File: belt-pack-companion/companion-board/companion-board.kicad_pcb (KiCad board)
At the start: 2 copper layers, 29.4 x 47.2 mm, 64 parts, among them J1 Conn_01x18_Socket, J2 Conn_01x18_Socket, J4 Conn_01x03_Pin, Q1 MMBT3904, Q2 MMBT3904, U1 TLV320AIC3204, X1 YC24.576MUBCE2O

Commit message: PCB Updates
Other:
- board text added: "Heltec WiFi LoRa 32 v3 Companion Board Rev.1"
- board text added: "Heltec v3 Companion Rev.1"
- board text added: "Line Out"

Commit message: Board updates
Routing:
- net GND: vias 156 -> 153
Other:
- board text added: "Supported by"
- board text added: "https://github.com/PKCubed/LibreCom"

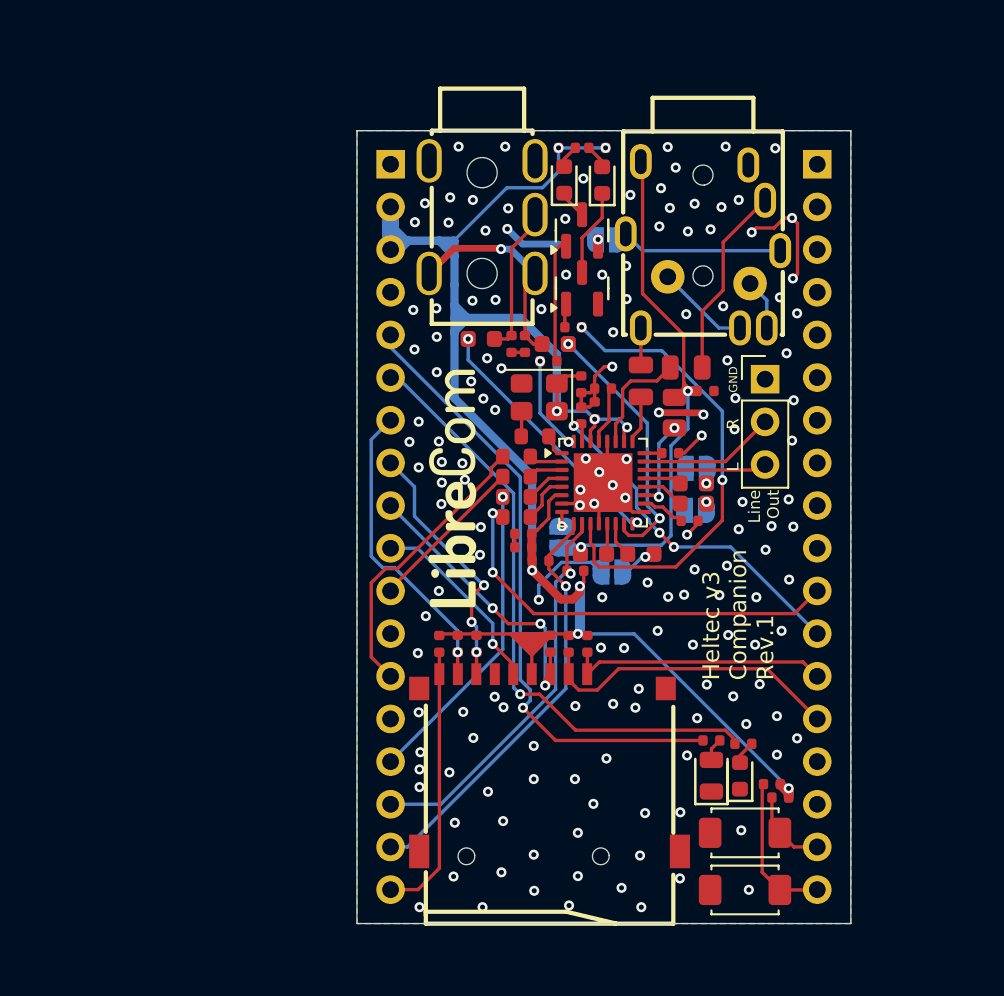
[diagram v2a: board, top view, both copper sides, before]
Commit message: Added more GPIO labels and started to add PTT button
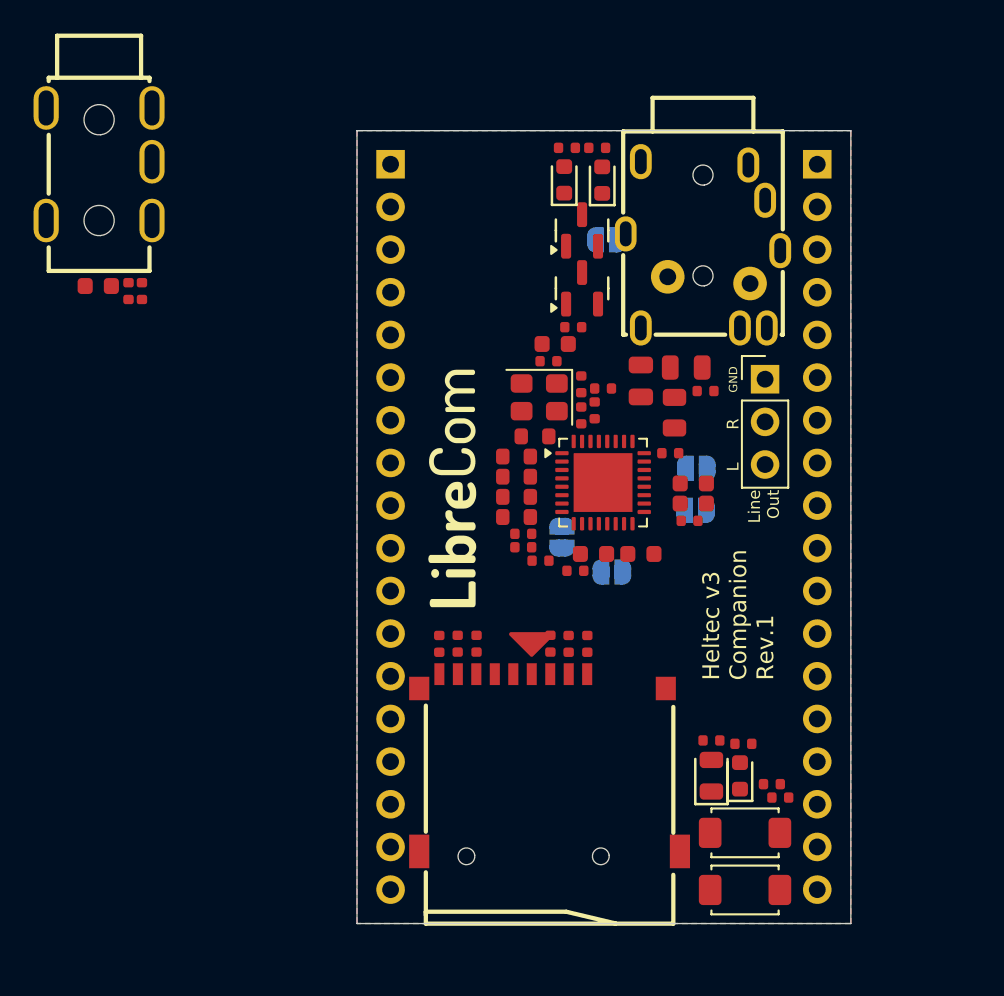
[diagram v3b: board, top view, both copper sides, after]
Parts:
- moved R33 23.0 mm to (95.1, 48.0)
- moved J3 23.0 mm to (93.3, 40.5)
- moved R32 23.0 mm to (95.9, 48.0)
- moved C11 23.0 mm to (93.3, 47.8)
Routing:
- net +3.3V: track 109.6 -> 0.00 mm, vias 9 -> 0
- net GND: track 39.8 -> 0.00 mm, vias 153 -> 0
- net LED_Green: track 37.3 -> 0.00 mm, vias 1 -> 0
- net LED_Red: track 36.4 -> 0.00 mm, vias 1 -> 0
- net MIC: track 34.6 -> 0.00 mm, vias 2 -> 0
- net Net-(U1-MISO/MFP4): track 28.2 -> 0.00 mm, vias 2 -> 0
- net I^{2}C_SCL: track 25.2 -> 0.00 mm, vias 1 -> 0
- net I^{2}S_MIC_DATA: track 25.1 -> 0.00 mm, vias 2 -> 0
- net I^{2}C_SDA: track 23.6 -> 0.00 mm, vias 1 -> 0
- net CODEC_RESET: track 21.9 -> 0.00 mm, vias 3 -> 0
- net I^{2}S_SPK_DATA: track 18.5 -> 0.00 mm, vias 1 -> 0
- net SD_DAT3: track 18.5 -> 0.00 mm
- net SD_DAT1: track 18.2 -> 0.00 mm, vias 1 -> 0
- net SD_CMD: track 17.8 -> 0.00 mm, vias 3 -> 0
- net I^{2}S_WCLK: track 17.2 -> 0.00 mm
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
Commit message: Finished laying out components in new layout, ready to route
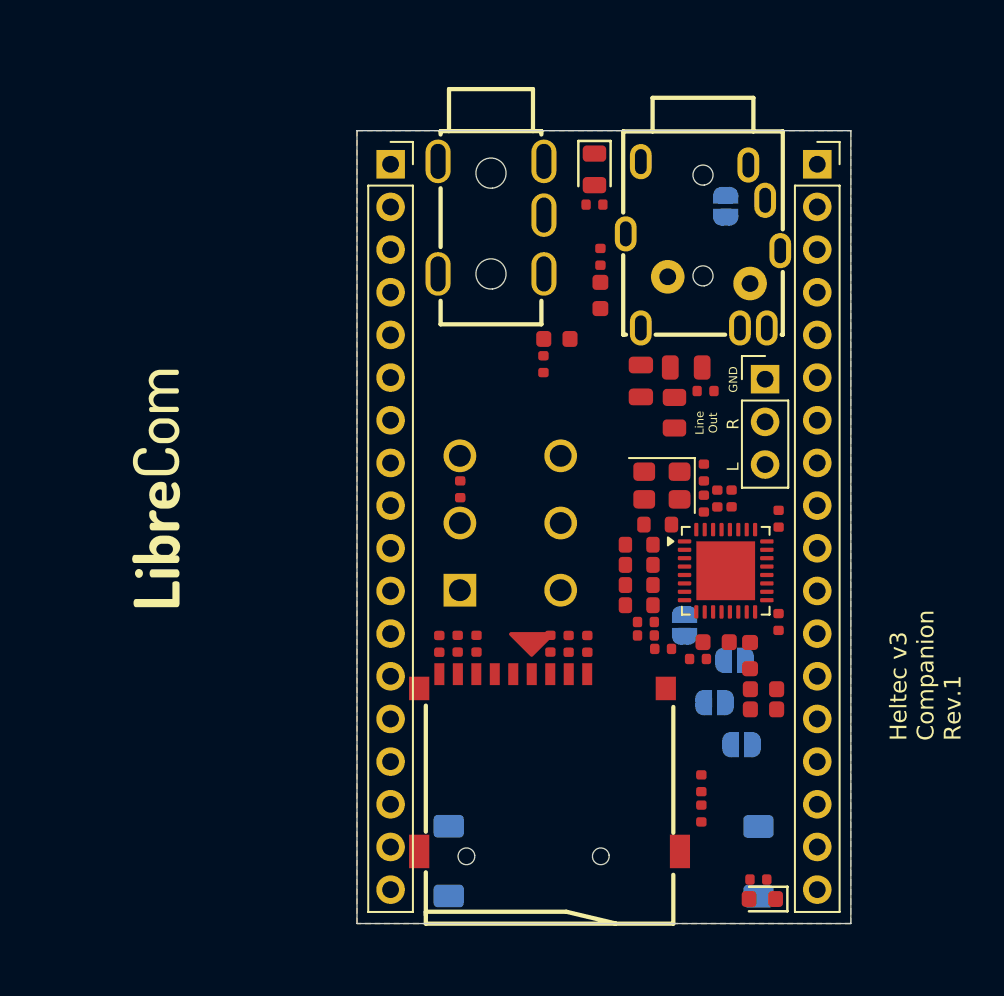
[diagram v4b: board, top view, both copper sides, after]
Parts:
- removed D2: White, PCM_JLCPCB:D_0603
- removed D3: Yellow, PCM_JLCPCB:D_0603
- removed Q1, Q2: MMBT3904, PCM_JLCPCB:Q_SOT-23
- removed R19, R22: 1kΩ, PCM_JLCPCB:R_0402
- removed R20, R21: 470Ω, PCM_JLCPCB:R_0402
- added R24: 10kΩ, PCM_JLCPCB:R_0402, F.Cu at (114.8, 59.8)
- added S3: MPBS-22H01-F14, Footprints:MPBS22H01F14, B.Cu at (114.8, 65.9)
- J1, J2: moved to F.Cu
- S1, S2: moved to B.Cu
- moved D4 36.8 mm to (122.8, 40.8), turned to -90 degrees
- moved R17 32.6 mm to (122.8, 42.9), turned to 180 degrees
- moved C11 29.9 mm to (123.2, 48.3), turned to 90 degrees
- moved R33 28.2 mm to (123.2, 46.0), turned to 90 degrees
- moved J1 25.4 mm to (136.1, 40.5), turned to 0 degrees
- moved J2 25.4 mm to (110.7, 40.5), turned to 0 degrees
- moved R32 24.3 mm to (119.8, 52.4)
- moved J3 23.5 mm to (116.7, 43.7)
- moved S1 17.7 mm to (114.2, 82.0), turned to -90 degrees
- moved JP4 16.7 mm to (131.6, 75.0)
- moved C14 14.1 mm to (132.9, 73.0), turned to 180 degrees
- moved C13 11.8 mm to (132.9, 71.8), turned to 180 degrees
- moved JP3 11.5 mm to (130.0, 72.5)
- moved C9 10.1 mm to (131.0, 60.4), turned to 90 degrees
- moved C1 8.99 mm to (130.2, 60.4)
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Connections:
- J2 pad 15: unconnected-(J2-Pin_15-Pad15) -> Button_PTT

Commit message: board progress
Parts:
- moved R5 2.11 mm to (124.5, 62.0)
- moved C4 1.29 mm to (133.1, 66.6)
- moved C1 1.01 mm to (129.1, 60.4)
- moved C15 1.01 mm to (128.3, 58.9)
- moved C2 1.01 mm to (124.9, 67.8)
- moved C3 1.01 mm to (124.9, 68.5)
- moved C9 1.01 mm to (130.0, 60.4)
- moved R1 1.01 mm to (124.5, 65.5)
- moved R13 1.01 mm to (128.3, 60.7)
- moved R2 1.01 mm to (124.5, 66.8)
- moved R3 1.01 mm to (124.5, 63.1)
- moved R4 1.01 mm to (124.5, 64.3)
- moved R7 1.01 mm to (125.9, 69.3)
- moved U1 1.01 mm to (129.6, 64.7)
- moved X1 1.01 mm to (125.8, 59.6)
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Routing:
- net I^{2}C_SDA: track 0.00 -> 3.15 mm
- net Net-(U1-DOUT/MFP2): track 0.00 -> 2.84 mm
- net I^{2}C_SCL: track 0.00 -> 2.81 mm
- net Net-(U1-DIN/MFP1): track 0.00 -> 2.34 mm
- net I^{2}S_MCLK: track 0.00 -> 2.30 mm
- net Net-(U1-WCLK): track 0.00 -> 2.05 mm
- net Net-(U1-BCLK): track 0.00 -> 2.00 mm
- net Net-(U1-DVDD): track 0.00 -> 1.60 mm
- net +3.3V: track 0.00 -> 1.45 mm
- net CODEC_RESET: track 0.00 -> 1.07 mm
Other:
- copper layers 2 -> 4

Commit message: PCB Progress
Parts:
- moved J4 0.56 mm to (133.6, 53.2)
- moved C9 0.53 mm to (130.3, 60.0)
- moved C1 0.40 mm to (129.1, 60.0)
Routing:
- net I^{2}C_SDA: track 3.15 -> 0.00 mm
- net Net-(U1-DOUT/MFP2): track 2.84 -> 0.00 mm
- net I^{2}C_SCL: track 2.81 -> 0.00 mm
- net Net-(U1-DIN/MFP1): track 2.34 -> 0.00 mm
- net I^{2}S_MCLK: track 2.30 -> 0.00 mm
- net Net-(U1-WCLK): track 2.05 -> 0.00 mm
- net Net-(U1-BCLK): track 2.00 -> 0.00 mm
- net Net-(U1-DVDD): track 1.60 -> 0.00 mm
- net +3.3V: track 1.45 -> 0.00 mm
- net CODEC_RESET: track 1.07 -> 0.00 mm
- removed copper zone on B.Cu, net GND
- removed copper zone on F.Cu, net GND

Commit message: pcb updates
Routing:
- net +3.3V: track 0.00 -> 88.8 mm, vias 0 -> 1
- net MIC: track 0.00 -> 51.4 mm, vias 0 -> 2
- net SD_DAT0: track 0.00 -> 36.1 mm, vias 0 -> 2
- net LED_Red: track 0.00 -> 32.6 mm, vias 0 -> 1
- net SD_DETECT: track 0.00 -> 30.6 mm, vias 0 -> 1
- net SD_DAT1: track 0.00 -> 30.3 mm, vias 0 -> 1
- net GND: track 0.00 -> 27.4 mm, vias 0 -> 27
- net CODEC_RESET: track 0.00 -> 26.6 mm, vias 0 -> 1
- net Net-(U1-IN2_L): track 0.00 -> 26.5 mm, vias 0 -> 2
- net SD_CMD: track 0.00 -> 25.9 mm, vias 0 -> 2
- net Button_2: track 0.00 -> 25.6 mm, vias 0 -> 1
- net Button_1: track 0.00 -> 25.2 mm, vias 0 -> 1
- net SD_CLK: track 0.00 -> 22.8 mm, vias 0 -> 1
- net I^{2}C_SDA: track 0.00 -> 22.7 mm
- net Net-(U1-IN2_R): track 0.00 -> 22.6 mm, vias 0 -> 2
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- added copper zone on In1.Cu, net +3.3V
- added copper zone on In2.Cu, net +3.3V
- added copper zone on B.Cu, net GND
- added copper zone on F.Cu, net GND

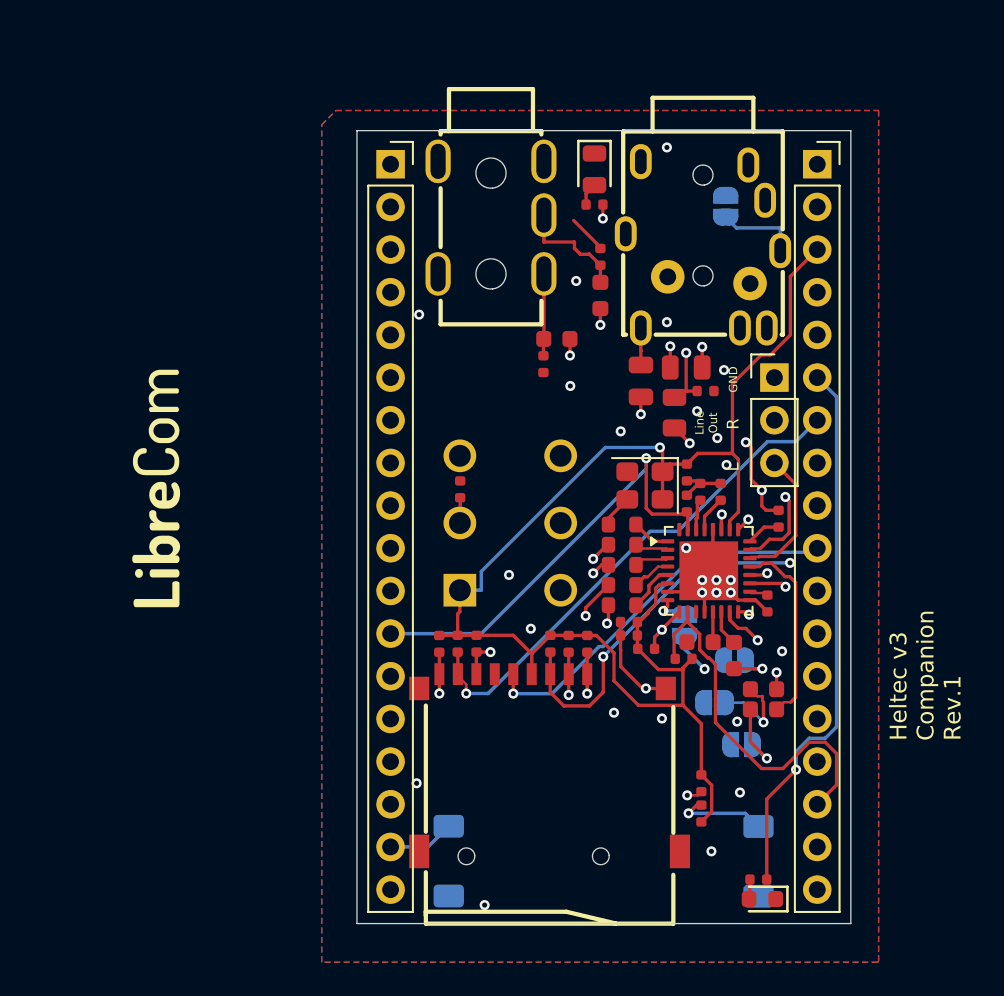
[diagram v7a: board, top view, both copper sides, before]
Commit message: Started to manually route... freerouting is just causing more problems than it's solving
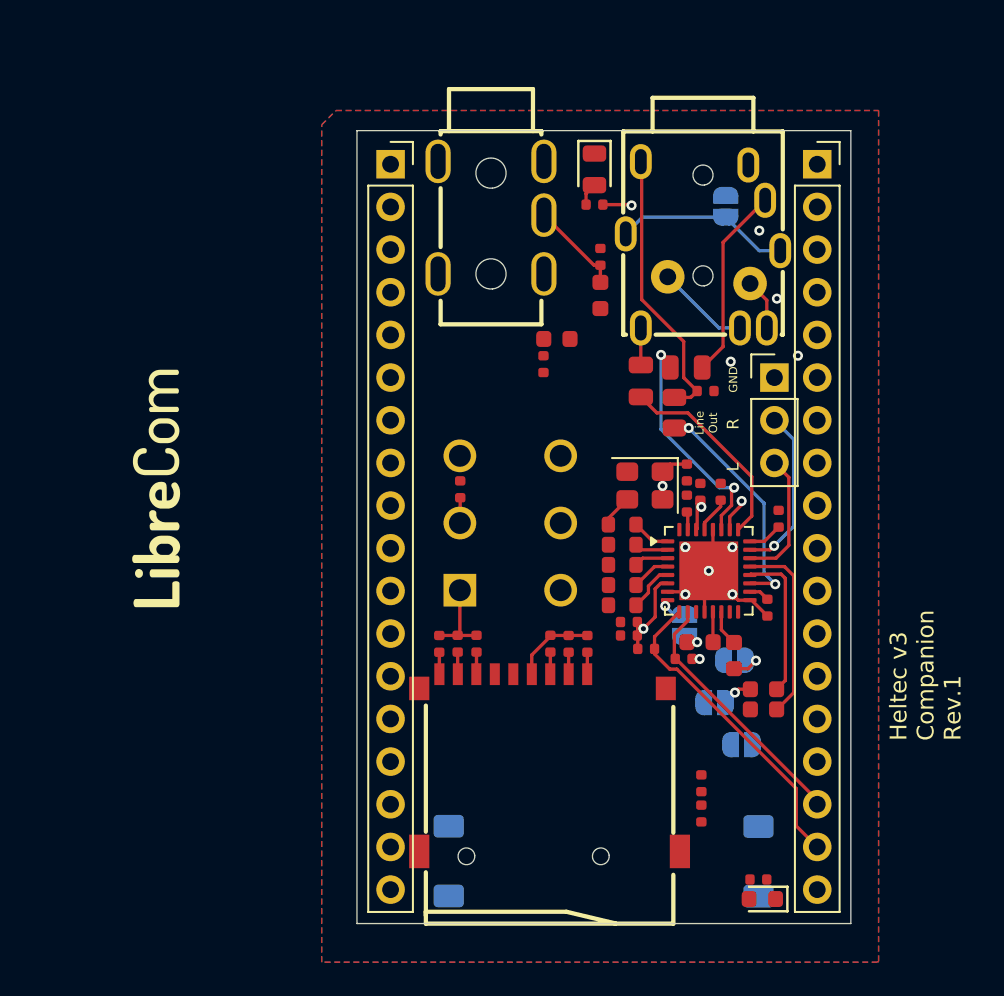
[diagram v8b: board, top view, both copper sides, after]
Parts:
- moved C4 0.25 mm to (133.1, 66.9)
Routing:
- net +3.3V: track 88.8 -> 32.7 mm, vias 1 -> 9
- net SD_DAT0: track 36.1 -> 1.32 mm, vias 2 -> 0
- net MIC: track 51.4 -> 18.1 mm, vias 2 -> 1
- net LED_Red: track 32.6 -> 0.00 mm, vias 1 -> 0
- net SD_DETECT: track 30.6 -> 1.31 mm, vias 1 -> 0
- net SD_DAT1: track 30.3 -> 1.32 mm, vias 1 -> 0
- net Net-(U1-IN2_L): track 26.5 -> 0.00 mm, vias 2 -> 0
- net Button_2: track 25.6 -> 0.00 mm, vias 1 -> 0
- net CODEC_RESET: track 26.6 -> 1.07 mm, vias 1 -> 0
- net Button_1: track 25.2 -> 0.00 mm, vias 1 -> 0
- net SD_CMD: track 25.9 -> 1.32 mm, vias 2 -> 0
- net SD_CLK: track 22.8 -> 0.00 mm, vias 1 -> 0
- net Net-(U1-IN2_R): track 22.6 -> 0.00 mm, vias 2 -> 0
- net I^{2}S_BCLK: track 21.5 -> 0.00 mm, vias 2 -> 0
- net GND: track 27.4 -> 7.30 mm, vias 27 -> 5
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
